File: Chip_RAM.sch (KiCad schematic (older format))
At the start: 51 parts, among them U204 74F04, U251 74F373, U252 74F86, U253 74F646, U254 74F646, U255 74F464, U256 74F464, U257 74F245, U258 74F245, U259 MCM41256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

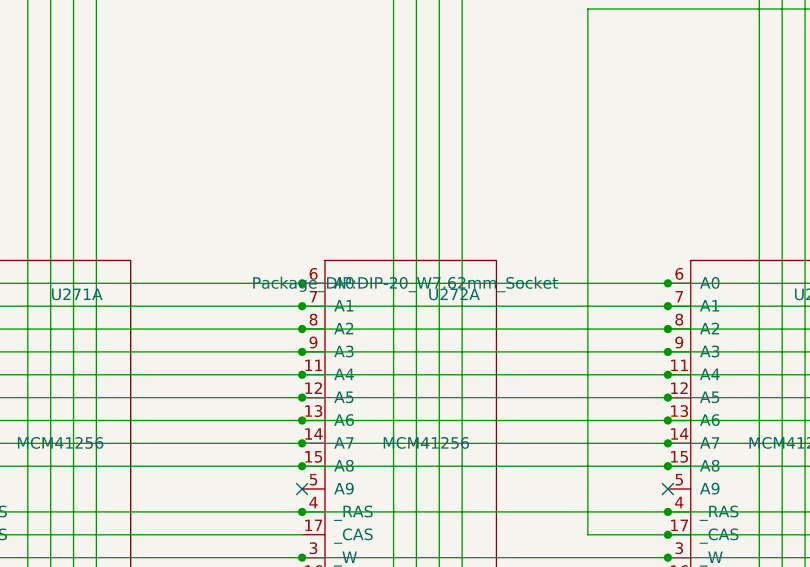
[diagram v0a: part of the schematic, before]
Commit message: Minor changes to schematics
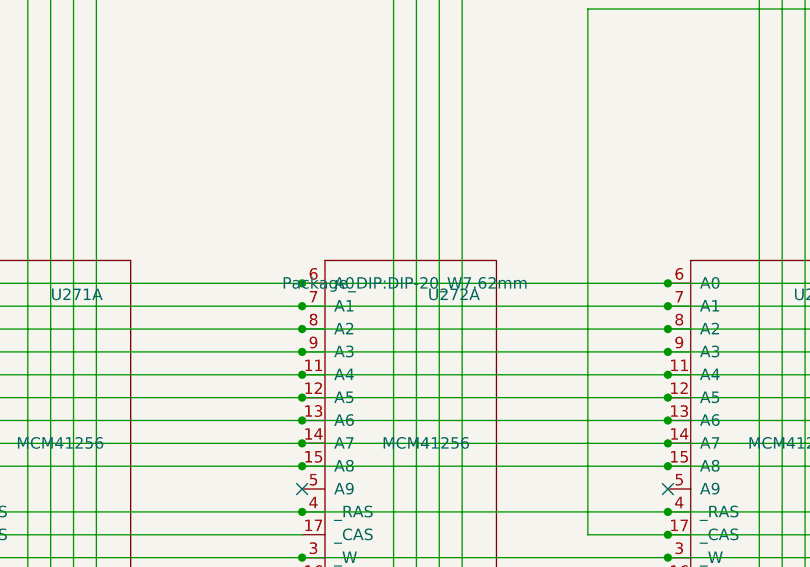
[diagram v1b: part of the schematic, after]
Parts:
- U267, U268, U269, U270, U271, U272, U273, U274: footprint Package_DIP:DIP-20_W7.62mm_Socket -> Package_DIP:DIP-20_W7.62mm
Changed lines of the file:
@@
 F 0 "U271" H 13050 11850 50  0000 L CNN
 F 1 "MCM41256" H 12900 11200 50  0000 L CNN
-F 2 "Package_DIP:DIP-20_W7.62mm_Socket" H 13000 11900 50  0001 C CNN
+F 2 "Package_DIP:DIP-20_W7.62mm" H 13000 11900 50  0001 C CNN
 F 3 "" H 13000 11900 50  0001 C CNN
 	1    13050 11250
@@
 F 0 "U272" H 14700 11850 50  0000 L CNN
 F 1 "MCM41256" H 14500 11200 50  0000 L CNN
-F 2 "Package_DIP:DIP-20_W7.62mm_Socket" H 14600 11900 50  0000 C CNN
+F 2 "Package_DIP:DIP-20_W7.62mm" H 14600 11900 50  0000 C CNN
 F 3 "" H 14600 11900 50  0001 C CNN
 	1    14650 11250
@@
 F 0 "U273" H 16300 11850 50  0000 L CNN
 F 1 "MCM41256" H 16100 11200 50  0000 L CNN
-F 2 "Package_DIP:DIP-20_W7.62mm_Socket" H 16200 11900 50  0001 C CNN
+F 2 "Package_DIP:DIP-20_W7.62mm" H 16200 11900 50  0001 C CNN
 F 3 "" H 16200 11900 50  0001 C CNN
 	1    16250 11250
@@
 F 0 "U274" H 17800 11850 50  0000 L CNN
 F 1 "MCM41256" H 17600 11200 50  0000 L CNN
-F 2 "Package_DIP:DIP-20_W7.62mm_Socket" H 17700 11900 50  0001 C CNN
+F 2 "Package_DIP:DIP-20_W7.62mm" H 17700 11900 50  0001 C CNN
 F 3 "" H 17700 11900 50  0001 C CNN
 	1    17750 11250
@@
 F 0 "U267" H 13050 6150 50  0000 L CNN
 F 1 "MCM41256" H 12900 5500 50  0000 L CNN
-F 2 "Package_DIP:DIP-20_W7.62mm_Socket" H 13000 6200 50  0001 C CNN
+F 2 "Package_DIP:DIP-20_W7.62mm" H 13000 6200 50  0001 C CNN
 F 3 "" H 13000 6200 50  0001 C CNN
 	1    13050 5550
@@
 F 0 "U268" H 14700 6150 50  0000 L CNN
 F 1 "MCM41256" H 14500 5500 50  0000 L CNN
-F 2 "Package_DIP:DIP-20_W7.62mm_Socket" H 14600 6200 50  0001 C CNN
+F 2 "Package_DIP:DIP-20_W7.62mm" H 14600 6200 50  0001 C CNN
 F 3 "" H 14600 6200 50  0001 C CNN
 	1    14650 5550
@@
 F 0 "U269" H 16300 6150 50  0000 L CNN
 F 1 "MCM41256" H 16100 5500 50  0000 L CNN
-F 2 "Package_DIP:DIP-20_W7.62mm_Socket" H 16200 6200 50  0001 C CNN
+F 2 "Package_DIP:DIP-20_W7.62mm" H 16200 6200 50  0001 C CNN
 F 3 "" H 16200 6200 50  0001 C CNN
 	1    16250 5550
@@
 F 0 "U270" H 17800 6150 50  0000 L CNN
 F 1 "MCM41256" H 17600 5500 50  0000 L CNN
-F 2 "Package_DIP:DIP-20_W7.62mm_Socket" H 17700 6200 50  0001 C CNN
+F 2 "Package_DIP:DIP-20_W7.62mm" H 17700 6200 50  0001 C CNN
 F 3 "" H 17700 6200 50  0001 C CNN
 	1    17750 5550
@@
 F 0 "U267" H 8750 14600 50  0000 L CNN
 F 1 "MCM41256" H 8700 14000 50  0000 L CNN
-F 2 "Package_DIP:DIP-20_W7.62mm_Socket" H 8600 15000 50  0001 C CNN
+F 2 "Package_DIP:DIP-20_W7.62mm" H 8600 15000 50  0001 C CNN
 F 3 "" H 8600 15000 50  0001 C CNN
 	2    8650 14350
@@
 F 0 "U268" H 9950 14600 50  0000 L CNN
 F 1 "MCM41256" H 9900 14000 50  0000 L CNN
-F 2 "Package_DIP:DIP-20_W7.62mm_Socket" H 9800 15000 50  0001 C CNN
+F 2 "Package_DIP:DIP-20_W7.62mm" H 9800 15000 50  0001 C CNN
 F 3 "" H 9800 15000 50  0001 C CNN
 	2    9850 14350
@@
 F 0 "U269" H 11150 14600 50  0000 L CNN
 F 1 "MCM41256" H 11100 14000 50  0000 L CNN
-F 2 "Package_DIP:DIP-20_W7.62mm_Socket" H 11000 15000 50  0001 C CNN
+F 2 "Package_DIP:DIP-20_W7.62mm" H 11000 15000 50  0001 C CNN
 F 3 "" H 11000 15000 50  0001 C CNN
 	2    11050 14350
@@
 F 0 "U270" H 12350 14600 50  0000 L CNN
 F 1 "MCM41256" H 12300 14000 50  0000 L CNN
-F 2 "Package_DIP:DIP-20_W7.62mm_Socket" H 12200 15000 50  0001 C CNN
+F 2 "Package_DIP:DIP-20_W7.62mm" H 12200 15000 50  0001 C CNN
 F 3 "" H 12200 15000 50  0001 C CNN
 	2    12250 14350
@@
 F 0 "U271" H 13600 14600 50  0000 L CNN
 F 1 "MCM41256" H 13550 14000 50  0000 L CNN
-F 2 "Package_DIP:DIP-20_W7.62mm_Socket" H 13450 15000 50  0001 C CNN
+F 2 "Package_DIP:DIP-20_W7.62mm" H 13450 15000 50  0001 C CNN
 F 3 "" H 13450 15000 50  0001 C CNN
 	2    13500 14350
@@
 F 0 "U272" H 14800 14600 50  0000 L CNN
 F 1 "MCM41256" H 14750 14000 50  0000 L CNN
-F 2 "Package_DIP:DIP-20_W7.62mm_Socket" H 14650 15000 50  0001 C CNN
+F 2 "Package_DIP:DIP-20_W7.62mm" H 14650 15000 50  0001 C CNN
 F 3 "" H 14650 15000 50  0001 C CNN
 	2    14700 14350
@@
 F 0 "U273" H 16000 14600 50  0000 L CNN
 F 1 "MCM41256" H 15950 14000 50  0000 L CNN
-F 2 "Package_DIP:DIP-20_W7.62mm_Socket" H 15850 15000 50  0001 C CNN
+F 2 "Package_DIP:DIP-20_W7.62mm" H 15850 15000 50  0001 C CNN
 F 3 "" H 15850 15000 50  0001 C CNN
 	2    15900 14350
@@
 F 0 "U274" H 17200 14600 50  0000 L CNN
 F 1 "MCM41256" H 17150 14000 50  0000 L CNN
-F 2 "Package_DIP:DIP-20_W7.62mm_Socket" H 17050 15000 50  0001 C CNN
+F 2 "Package_DIP:DIP-20_W7.62mm" H 17050 15000 50  0001 C CNN
 F 3 "" H 17050 15000 50  0001 C CNN
 	2    17100 14350
